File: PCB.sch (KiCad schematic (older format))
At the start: 22 parts

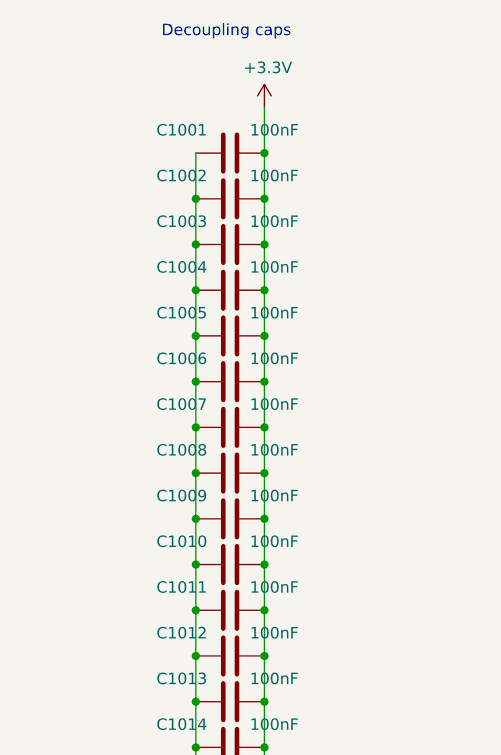
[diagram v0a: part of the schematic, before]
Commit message: Change optocoupler types, improve ground planes and a lot of other smaller fixes
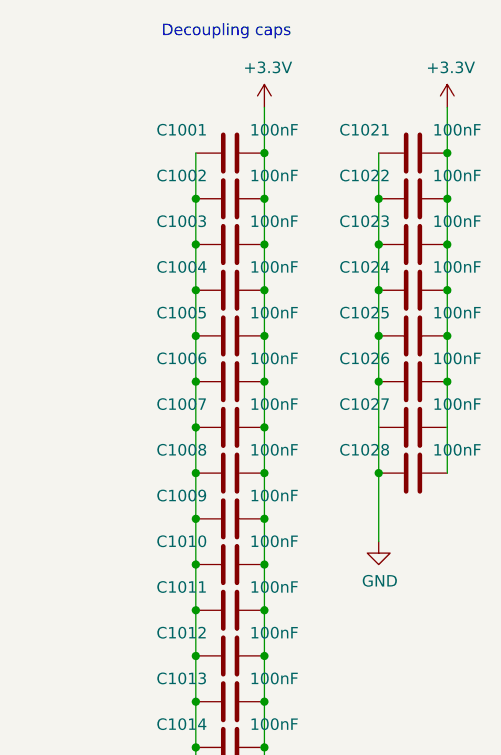
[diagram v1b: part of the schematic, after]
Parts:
- added C1021, C1022, C1023, C1024, C1025, C1026, C1027, C1028: 100nF, Capacitor_SMD:C_0402_1005Metric, symbol Device:C
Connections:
- net +3V3: now also C1021.2, C1022.2, C1023.2, C1024.2, C1025.2, C1026.2, C1027.2, C1028.2
- net GND: now also C1021.1, C1022.1, C1023.1, C1024.1, C1025.1, C1026.1, C1027.1, C1028.1
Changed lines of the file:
@@
 	1    0    0    -1
 $EndComp
+$Comp
+L Device:C C?
+U 1 1 5FC378F5
+P 4550 1850
+AR Path="/5D6F1C7C/5FC378F5" Ref="C?"  Part="1"
+AR Path="/5C348474/5FC378F5" Ref="C?"  Part="1"
+AR Path="/5F733BA4/5FC378F5" Ref="C?"  Part="1"
+AR Path="/5FC0C355/5FC378F5" Ref="C1021"  Part="1"
+F 0 "C1021" V 4450 1950 50  0000 L CNN
+F 1 "100nF" V 4450 1550 50  0000 L CNN
+F 2 "Capacitor_SMD:C_0402_1005Metric" H 4588 1700 50  0001 C CNN
+F 3 "~" H 4550 1850 50  0001 C CNN
+F 4 "C1525" H 4550 1850 50  0001 C CNN "LCSC"
+	1    4550 1850
+	0    -1   1    0
+$EndComp
+$Comp
+L Device:C C?
+U 1 1 5FC378FC
+P 4550 2050
+AR Path="/5D6F1C7C/5FC378FC" Ref="C?"  Part="1"
+AR Path="/5C348474/5FC378FC" Ref="C?"  Part="1"
+AR Path="/5F733BA4/5FC378FC" Ref="C?"  Part="1"
+AR Path="/5FC0C355/5FC378FC" Ref="C1022"  Part="1"
+F 0 "C1022" V 4450 2150 50  0000 L CNN
+F 1 "100nF" V 4450 1750 50  0000 L CNN
+F 2 "Capacitor_SMD:C_0402_1005Metric" H 4588 1900 50  0001 C CNN
+F 3 "~" H 4550 2050 50  0001 C CNN
+F 4 "C1525" H 4550 2050 50  0001 C CNN "LCSC"
+	1    4550 2050
+	0    -1   1    0
+$EndComp
+$Comp
+L Device:C C?
+U 1 1 5FC37903
+P 4550 2250
+AR Path="/5D6F1C7C/5FC37903" Ref="C?"  Part="1"
+AR Path="/5C348474/5FC37903" Ref="C?"  Part="1"
+AR Path="/5F733BA4/5FC37903" Ref="C?"  Part="1"
+AR Path="/5FC0C355/5FC37903" Ref="C1023"  Part="1"
+F 0 "C1023" V 4450 2350 50  0000 L CNN
+F 1 "100nF" V 4450 1950 50  0000 L CNN
+F 2 "Capacitor_SMD:C_0402_1005Metric" H 4588 2100 50  0001 C CNN
+F 3 "~" H 4550 2250 50  0001 C CNN
+F 4 "C1525" H 4550 2250 50  0001 C CNN "LCSC"
+	1    4550 2250
+	0    -1   1    0
+$EndComp
+$Comp
+L Device:C C?
+U 1 1 5FC3790A
+P 4550 2450
+AR Path="/5D6F1C7C/5FC3790A" Ref="C?"  Part="1"
+AR Path="/5C348474/5FC3790A" Ref="C?"  Part="1"
+AR Path="/5F733BA4/5FC3790A" Ref="C?"  Part="1"
+AR Path="/5FC0C355/5FC3790A" Ref="C1024"  Part="1"
+F 0 "C1024" V 4450 2550 50  0000 L CNN
+F 1 "100nF" V 4450 2150 50  0000 L CNN
+F 2 "Capacitor_SMD:C_0402_1005Metric" H 4588 2300 50  0001 C CNN
+F 3 "~" H 4550 2450 50  0001 C CNN
+F 4 "C1525" H 4550 2450 50  0001 C CNN "LCSC"
+	1    4550 2450
+	0    -1   1    0
+$EndComp
+$Comp
+L Device:C C?
+U 1 1 5FC37911
+P 4550 2650
+AR Path="/5D6F1C7C/5FC37911" Ref="C?"  Part="1"
+AR Path="/5C348474/5FC37911" Ref="C?"  Part="1"
+AR Path="/5F733BA4/5FC37911" Ref="C?"  Part="1"
+AR Path="/5FC0C355/5FC37911" Ref="C1025"  Part="1"
+F 0 "C1025" V 4450 2750 50  0000 L CNN
+F 1 "100nF" V 4450 2350 50  0000 L CNN
+F 2 "Capacitor_SMD:C_0402_1005Metric" H 4588 2500 50  0001 C CNN
+F 3 "~" H 4550 2650 50  0001 C CNN
+F 4 "C1525" H 4550 2650 50  0001 C CNN "LCSC"
+	1    4550 2650
+	0    -1   1    0
+$EndComp
+Wire Wire Line
+	4400 1850 4400 2050
+Connection ~ 4400 2050
+Wire Wire Line
+	4400 2050 4400 2250
+Connection ~ 4400 2250
+Wire Wire Line
+	4400 2250 4400 2450
+Connection ~ 4400 2450
+Wire Wire Line
+	4400 2450 4400 2650
+Wire Wire Line
+	4400 2850 4400 3050
+Connection ~ 4700 1850
+Wire Wire Line
+	4700 1850 4700 1650
+Connection ~ 4700 2050
+Wire Wire Line
+	4700 2050 4700 1850
+Connection ~ 4700 2250
+Wire Wire Line
+	4700 2250 4700 2050
+Connection ~ 4700 2450
+Wire Wire Line
+	4700 2450 4700 2250
+Wire Wire Line
+	4700 2650 4700 2450
+$Comp
+L power:+3.3V #PWR01004
+U 1 1 5FC3792B
+P 4700 1650
+F 0 "#PWR01004" H 4700 1500 50  0001 C CNN
+F 1 "+3.3V" H 4715 1823 50  0000 C CNN
+F 2 "" H 4700 1650 50  0001 C CNN
+F 3 "" H 4700 1650 50  0001 C CNN
+	1    4700 1650
+	1    0    0    -1
+$EndComp
+$Comp
+L power:GND #PWR01003
+U 1 1 5FC39BF1
+P 4400 3550
+F 0 "#PWR01003" H 4400 3300 50  0001 C CNN
+F 1 "GND" H 4405 3377 50  0000 C CNN
+F 2 "" H 4400 3550 50  0001 C CNN
+F 3 "" H 4400 3550 50  0001 C CNN
+	1    4400 3550
+	1    0    0    -1
+$EndComp
+$Comp
+L Device:C C?
+U 1 1 5FC3D603
+P 4550 2850
+AR Path="/5D6F1C7C/5FC3D603" Ref="C?"  Part="1"
+AR Path="/5C348474/5FC3D603" Ref="C?"  Part="1"
+AR Path="/5F733BA4/5FC3D603" Ref="C?"  Part="1"
+AR Path="/5FC0C355/5FC3D603" Ref="C1026"  Part="1"
+F 0 "C1026" V 4450 2950 50  0000 L CNN
+F 1 "100nF" V 4450 2550 50  0000 L CNN
+F 2 "Capacitor_SMD:C_0402_1005Metric" H 4588 2700 50  0001 C CNN
+F 3 "~" H 4550 2850 50  0001 C CNN
+F 4 "C1525" H 4550 2850 50  0001 C CNN "LCSC"
+	1    4550 2850
+	0    -1   1    0
+$EndComp
+Wire Wire Line
+	4400 2650 4400 2850
+Wire Wire Line
+	4700 2850 4700 2650
+Connection ~ 4400 2850
+Connection ~ 4400 2650
+Connection ~ 4700 2650
+$Comp
+L Device:C C?
+U 1 1 5FC43B5E
+P 4550 3050
+AR Path="/5D6F1C7C/5FC43B5E" Ref="C?"  Part="1"
+AR Path="/5C348474/5FC43B5E" Ref="C?"  Part="1"
+AR Path="/5F733BA4/5FC43B5E" Ref="C?"  Part="1"
+AR Path="/5FC0C355/5FC43B5E" Ref="C1027"  Part="1"
+F 0 "C1027" V 4450 3150 50  0000 L CNN
+F 1 "100nF" V 4450 2750 50  0000 L CNN
+F 2 "Capacitor_SMD:C_0402_1005Metric" H 4588 2900 50  0001 C CNN
+F 3 "~" H 4550 3050 50  0001 C CNN
+F 4 "C1525" H 4550 3050 50  0001 C CNN "LCSC"
+	1    4550 3050
+	0    -1   1    0
+$EndComp
+Wire Wire Line
+	4700 3050 4700 2850
+Connection ~ 4700 2850
+Wire Wire Line
+	4400 3250 4400 3550
+Wire Wire Line
+	4400 3050 4400 3250
+$Comp
+L Device:C C?
+U 1 1 5FC49915
+P 4550 3250
+AR Path="/5D6F1C7C/5FC49915" Ref="C?"  Part="1"
+AR Path="/5C348474/5FC49915" Ref="C?"  Part="1"
+AR Path="/5F733BA4/5FC49915" Ref="C?"  Part="1"
+AR Path="/5FC0C355/5FC49915" Ref="C1028"  Part="1"
+F 0 "C1028" V 4450 3350 50  0000 L CNN
+F 1 "100nF" V 4450 2950 50  0000 L CNN
+F 2 "Capacitor_SMD:C_0402_1005Metric" H 4588 3100 50  0001 C CNN
+F 3 "~" H 4550 3250 50  0001 C CNN
+F 4 "C1525" H 4550 3250 50  0001 C CNN "LCSC"
+	1    4550 3250
+	0    -1   1    0
+$EndComp
+Wire Wire Line
+	4700 3250 4700 3050
+Connection ~ 4400 3250
 $EndSCHEMATC
